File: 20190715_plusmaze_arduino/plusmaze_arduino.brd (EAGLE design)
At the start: 61 x 40.6 mm, 11 parts

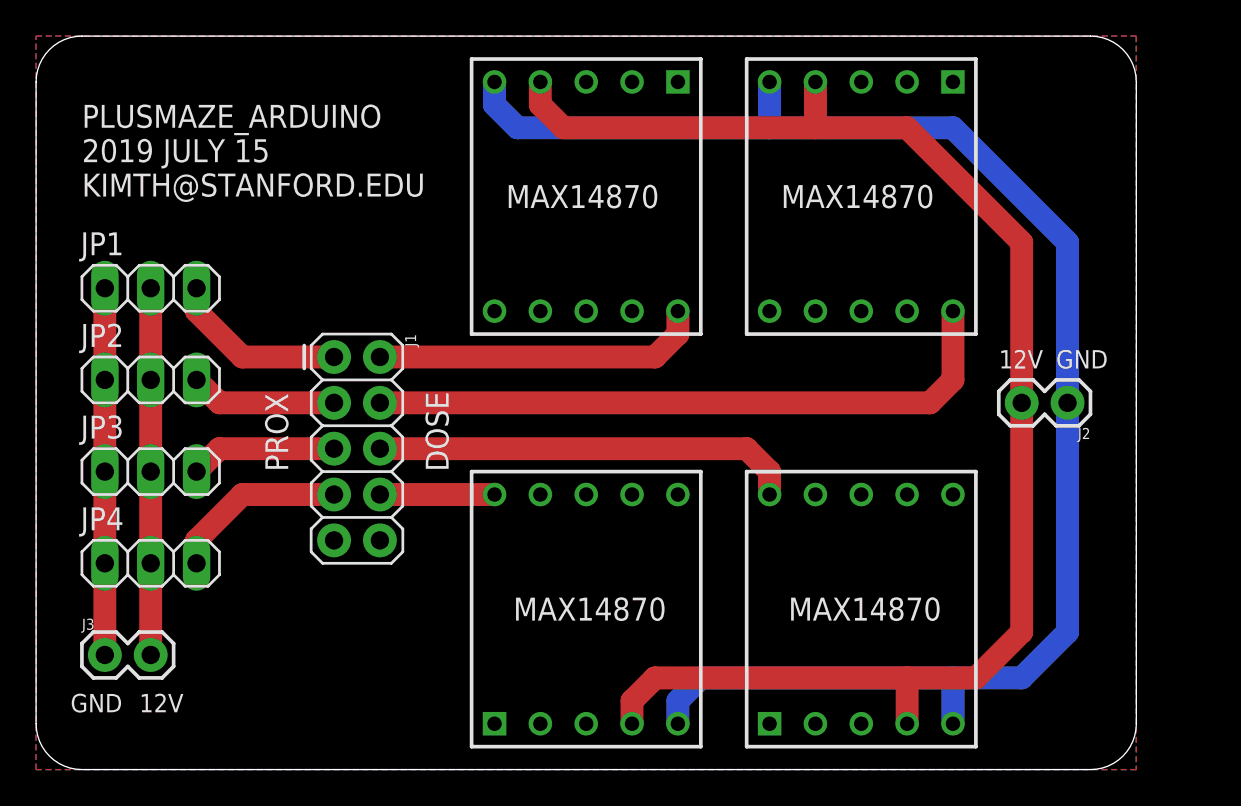
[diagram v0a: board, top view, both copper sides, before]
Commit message: Plusmaze Arduino add lickometers
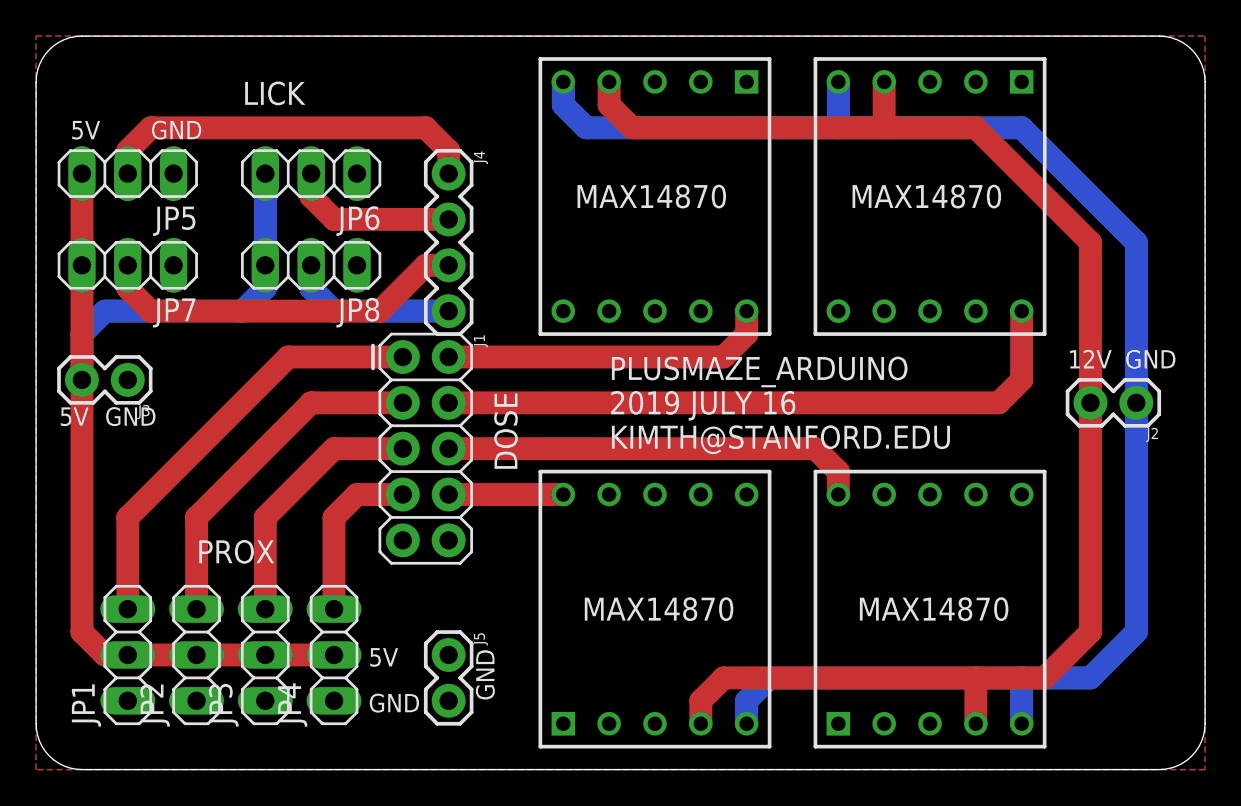
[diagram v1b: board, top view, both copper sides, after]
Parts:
- added J4: (no value), SparkFun-Connectors:1X04
- added J5: (no value), SparkFun-Connectors:1X02
- added JP5, JP6, JP7, JP8: (no value), pinhead:1X03
- moved JP1 20.4 mm to (5.08, 6.35), turned to 90 degrees
- moved JP2 15.5 mm to (8.89, 6.35), turned to 90 degrees
- moved J3 15.3 mm to (5.08, 21.6), turned to 180 degrees
- moved JP3 12.0 mm to (12.7, 6.35), turned to 90 degrees
- moved JP4 11.4 mm to (16.5, 6.35), turned to 90 degrees
- moved J2 3.81 mm to (61.0, 20.3)
- moved U$2 3.81 mm to (49.5, 31.8)
- moved U$3 3.81 mm to (49.5, 8.89)
- moved J1 3.81 mm to (20.3, 22.9)
- moved U$1 3.81 mm to (34.3, 31.8)
- moved U$4 3.81 mm to (34.3, 8.89)
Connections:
- new net LICK1: J4.1, JP5.2
- new net LICK2: J4.2, JP6.2
- new net LICK3: J4.3, JP7.2
- new net LICK4: J4.4, JP8.2
- net 5V: now also JP5.3, JP6.3, JP7.3, JP8.3
- net DGND: now also J5.1, J5.2, JP5.1, JP6.1, JP7.1, JP8.1
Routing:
- net 5V: track 20.3 -> 60.0 mm
- net LICK1: track 0.00 -> 21.4 mm
- net LICK3: track 0.00 -> 20.6 mm
- net DGND: track 20.3 -> 0.00 mm
- net PROX1: track 9.94 -> 24.0 mm
- net PROX2: track 8.15 -> 19.1 mm
- net LICK2: track 0.00 -> 9.42 mm
- net LICK4: track 0.00 -> 9.42 mm
- net PROX3: track 8.15 -> 14.3 mm
- net PROX4: track 9.94 -> 9.42 mm
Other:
- board size 61 x 40.6 mm -> 64.8 x 40.6 mm
- board text added: "5V"
- board text added: "LICK"
- board text added: "PLUSMAZE_ARDUINO 2019 JULY 16 KIMTH@STANFORD.EDU"
- board text removed: "PLUSMAZE_ARDUINO 2019 JULY 15 KIMTH@STANFORD.EDU"
